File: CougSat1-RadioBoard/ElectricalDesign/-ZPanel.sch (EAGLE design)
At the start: 0 parts

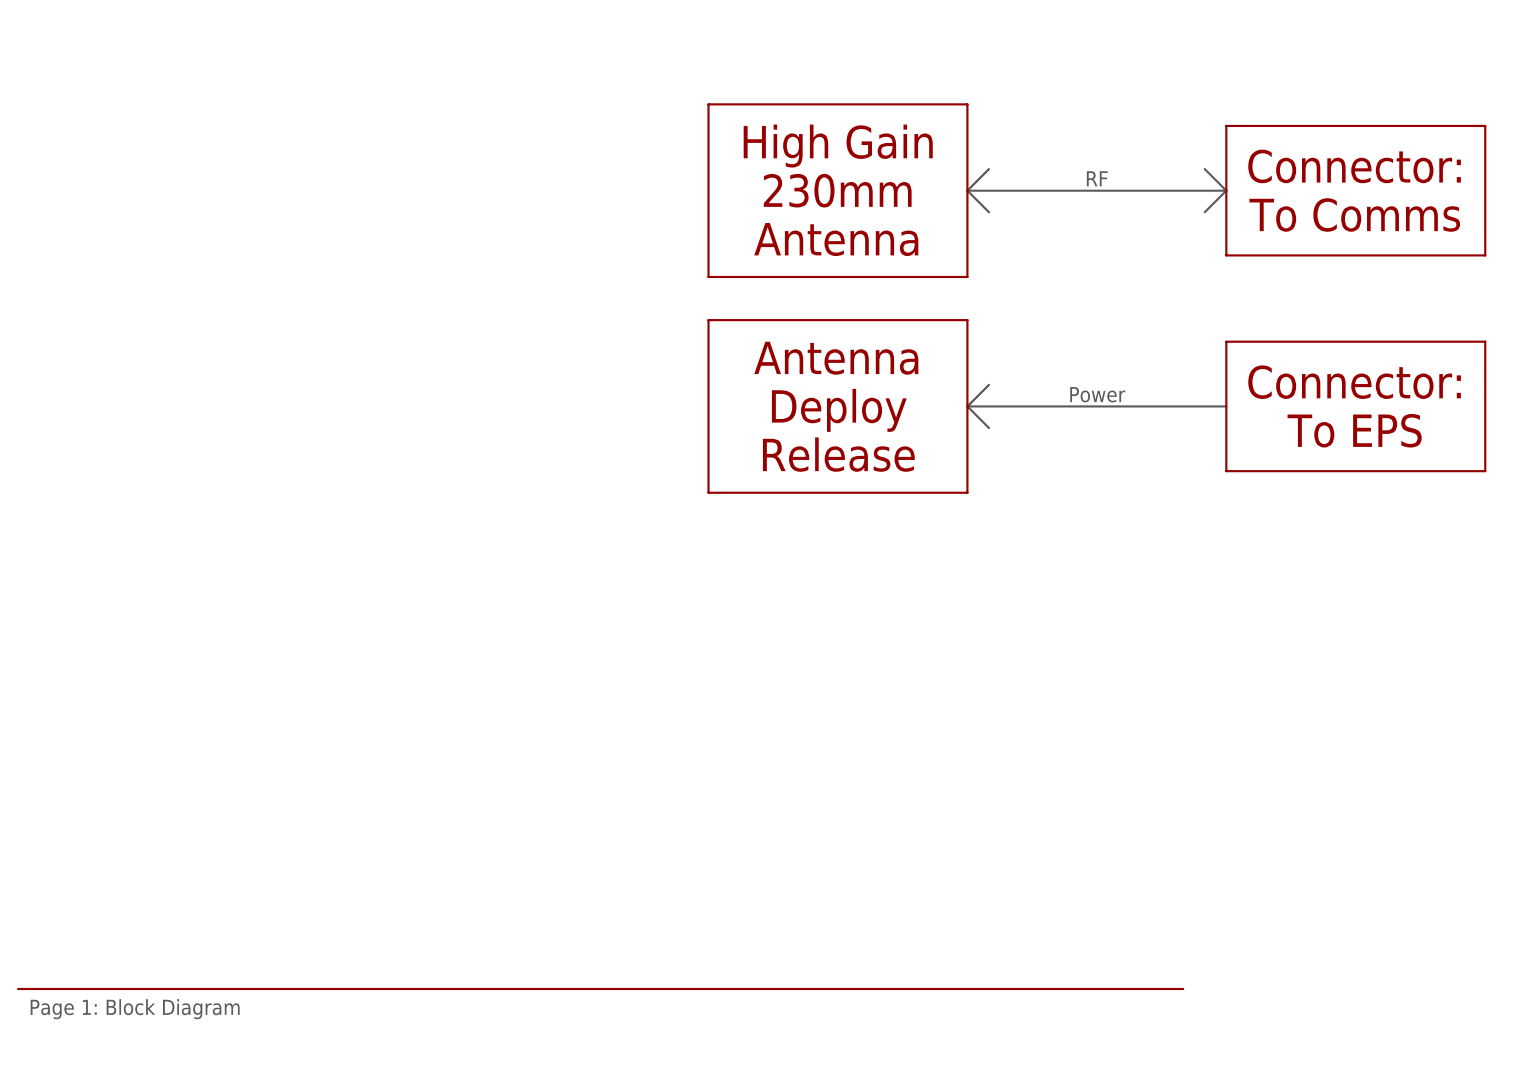
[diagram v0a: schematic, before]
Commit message: Added Photodiodes
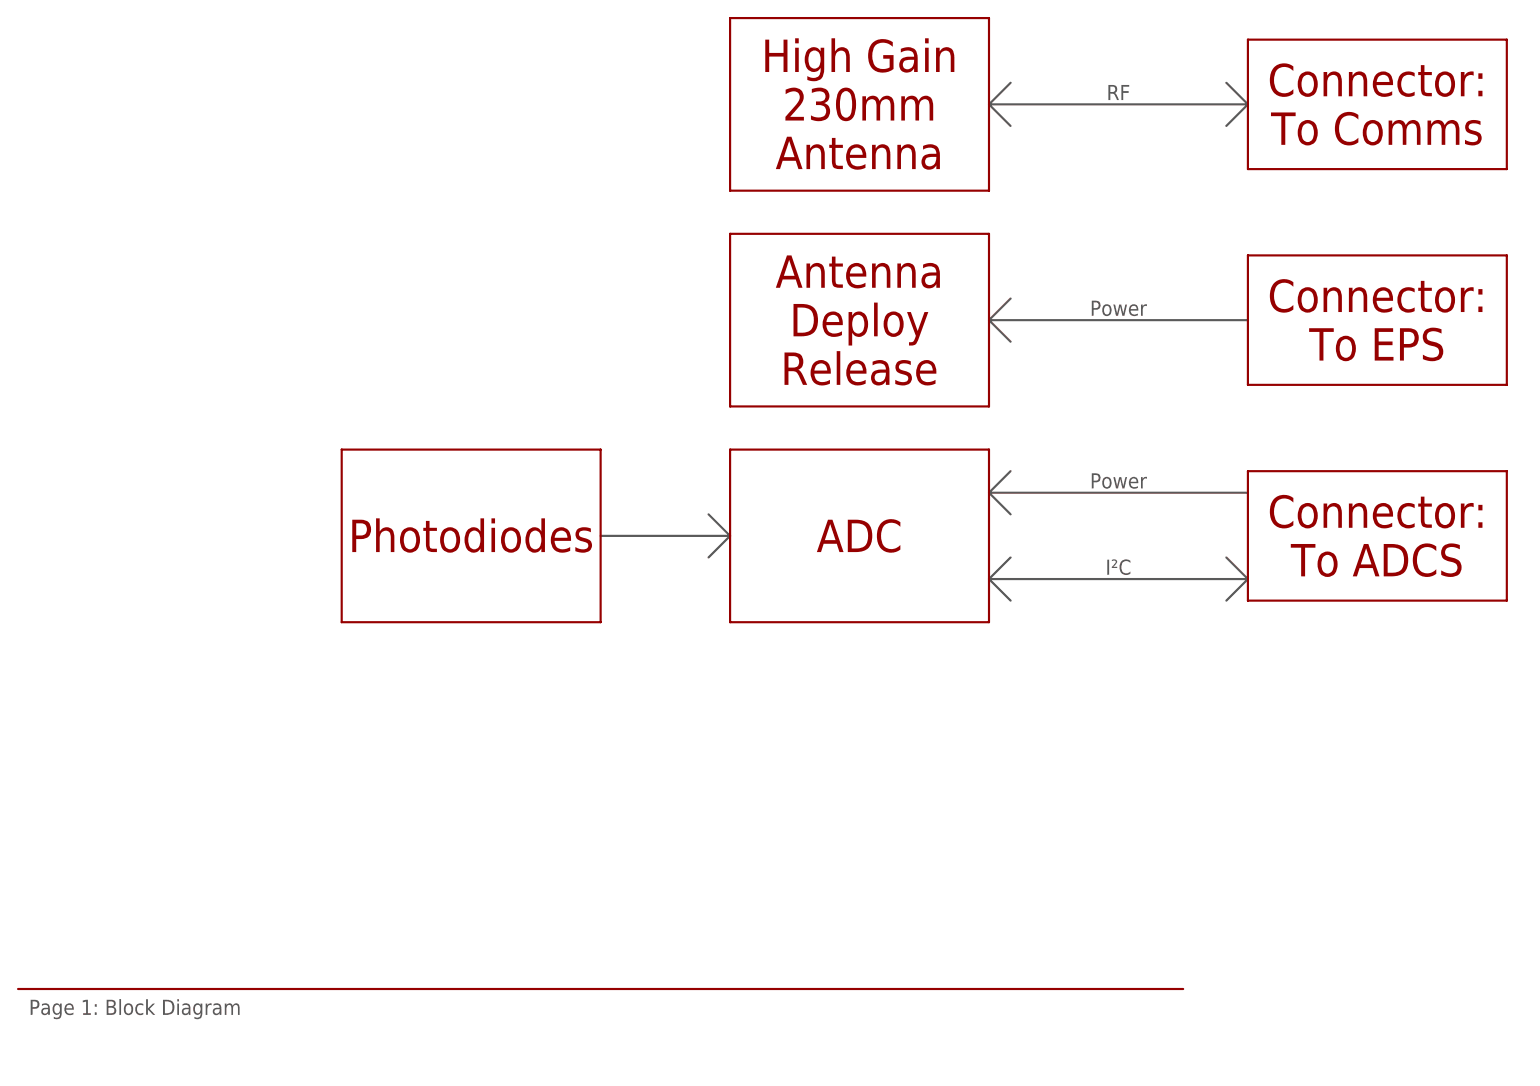
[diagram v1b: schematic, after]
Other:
- note added: "ADC"
- note added: "Connector: To ADCS"
- note added: "I²C"
- note added: "Photodiodes"
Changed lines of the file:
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@@
 <?xml version="1.0" encoding="utf-8"?>
 <!DOCTYPE eagle SYSTEM "eagle.dtd">
-<eagle version="9.2.1">
+<eagle version="9.2.2">
 <drawing>
 <settings>
@@
 <wire x1="137.16" y1="25.4" x2="0" y2="25.4" width="0.254" layer="94"/>
 <text x="1.27" y="24.13" size="1.778" layer="97" align="top-left">Page 1: Block Diagram</text>
-<text x="96.52" y="119.38" size="3.81" layer="94" align="center">High Gain
+<text x="99.06" y="129.54" size="3.81" layer="94" align="center">High Gain
 230mm
 Antenna</text>
-<text x="96.52" y="93.98" size="3.81" layer="94" align="center">Antenna
+<text x="99.06" y="104.14" size="3.81" layer="94" align="center">Antenna
 Deploy
 Release</text>
-<text x="157.48" y="119.38" size="3.81" layer="94" align="center">Connector:
+<text x="160.02" y="129.54" size="3.81" layer="94" align="center">Connector:
 To Comms</text>
-<text x="157.48" y="93.98" size="3.81" layer="94" align="center">Connector:
+<text x="160.02" y="104.14" size="3.81" layer="94" align="center">Connector:
 To EPS</text>
-<wire x1="142.24" y1="127" x2="172.72" y2="127" width="0.254" layer="94"/>
-<wire x1="172.72" y1="127" x2="172.72" y2="111.76" width="0.254" layer="94"/>
-<wire x1="172.72" y1="111.76" x2="142.24" y2="111.76" width="0.254" layer="94"/>
-<wire x1="142.24" y1="111.76" x2="142.24" y2="127" width="0.254" layer="94"/>
-<wire x1="142.24" y1="101.6" x2="142.24" y2="86.36" width="0.254" layer="94"/>
-<wire x1="142.24" y1="86.36" x2="172.72" y2="86.36" width="0.254" layer="94"/>
-<wire x1="172.72" y1="86.36" x2="172.72" y2="101.6" width="0.254" layer="94"/>
-<wire x1="172.72" y1="101.6" x2="142.24" y2="101.6" width="0.254" layer="94"/>
-<wire x1="81.28" y1="129.54" x2="111.76" y2="129.54" width="0.254" layer="94"/>
-<wire x1="111.76" y1="129.54" x2="111.76" y2="109.22" width="0.254" layer="94"/>
-<wire x1="111.76" y1="109.22" x2="81.28" y2="109.22" width="0.254" layer="94"/>
-<wire x1="81.28" y1="109.22" x2="81.28" y2="129.54" width="0.254" layer="94"/>
-<wire x1="81.28" y1="104.14" x2="111.76" y2="104.14" width="0.254" layer="94"/>
-<wire x1="81.28" y1="104.14" x2="81.28" y2="83.82" width="0.254" layer="94"/>
-<wire x1="111.76" y1="104.14" x2="111.76" y2="83.82" width="0.254" layer="94"/>
-<wire x1="81.28" y1="83.82" x2="111.76" y2="83.82" width="0.254" layer="94"/>
-<wire x1="111.76" y1="119.38" x2="142.24" y2="119.38" width="0.254" layer="97"/>
-<wire x1="139.7" y1="121.92" x2="142.24" y2="119.38" width="0.254" layer="97"/>
-<wire x1="142.24" y1="119.38" x2="139.7" y2="116.84" width="0.254" layer="97"/>
-<wire x1="114.3" y1="121.92" x2="111.76" y2="119.38" width="0.254" layer="97"/>
-<wire x1="111.76" y1="119.38" x2="114.3" y2="116.84" width="0.254" layer="97"/>
-<wire x1="142.24" y1="93.98" x2="111.76" y2="93.98" width="0.254" layer="97"/>
-<wire x1="114.3" y1="96.52" x2="111.76" y2="93.98" width="0.254" layer="97"/>
-<wire x1="111.76" y1="93.98" x2="114.3" y2="91.44" width="0.254" layer="97"/>
-<text x="127" y="119.888" size="1.778" layer="97" align="bottom-center">RF</text>
-<text x="127" y="94.488" size="1.778" layer="97" align="bottom-center">Power</text>
+<wire x1="144.78" y1="137.16" x2="175.26" y2="137.16" width="0.254" layer="94"/>
+<wire x1="175.26" y1="137.16" x2="175.26" y2="121.92" width="0.254" layer="94"/>
+<wire x1="175.26" y1="121.92" x2="144.78" y2="121.92" width="0.254" layer="94"/>
+<wire x1="144.78" y1="121.92" x2="144.78" y2="137.16" width="0.254" layer="94"/>
+<wire x1="144.78" y1="111.76" x2="144.78" y2="96.52" width="0.254" layer="94"/>
+<wire x1="144.78" y1="96.52" x2="175.26" y2="96.52" width="0.254" layer="94"/>
+<wire x1="175.26" y1="96.52" x2="175.26" y2="111.76" width="0.254" layer="94"/>
+<wire x1="175.26" y1="111.76" x2="144.78" y2="111.76" width="0.254" layer="94"/>
+<wire x1="83.82" y1="139.7" x2="114.3" y2="139.7" width="0.254" layer="94"/>
+<wire x1="114.3" y1="139.7" x2="114.3" y2="119.38" width="0.254" layer="94"/>
+<wire x1="114.3" y1="119.38" x2="83.82" y2="119.38" width="0.254" layer="94"/>
+<wire x1="83.82" y1="119.38" x2="83.82" y2="139.7" width="0.254" layer="94"/>
+<wire x1="83.82" y1="114.3" x2="114.3" y2="114.3" width="0.254" layer="94"/>
+<wire x1="83.82" y1="114.3" x2="83.82" y2="93.98" width="0.254" layer="94"/>
+<wire x1="114.3" y1="114.3" x2="114.3" y2="93.98" width="0.254" layer="94"/>
+<wire x1="83.82" y1="93.98" x2="114.3" y2="93.98" width="0.254" layer="94"/>
+<wire x1="114.3" y1="129.54" x2="144.78" y2="129.54" width="0.254" layer="97"/>
+<wire x1="142.24" y1="132.08" x2="144.78" y2="129.54" width="0.254" layer="97"/>
+<wire x1="144.78" y1="129.54" x2="142.24" y2="127" width="0.254" layer="97"/>
+<wire x1="116.84" y1="132.08" x2="114.3" y2="129.54" width="0.254" layer="97"/>
+<wire x1="114.3" y1="129.54" x2="116.84" y2="127" width="0.254" layer="97"/>
+<wire x1="144.78" y1="104.14" x2="114.3" y2="104.14" width="0.254" layer="97"/>
+<wire x1="116.84" y1="106.68" x2="114.3" y2="104.14" width="0.254" layer="97"/>
+<wire x1="114.3" y1="104.14" x2="116.84" y2="101.6" width="0.254" layer="97"/>
+<text x="129.54" y="130.048" size="1.778" layer="97" align="bottom-center">RF</text>
+<text x="129.54" y="104.648" size="1.778" layer="97" align="bottom-center">Power</text>
+<text x="99.06" y="78.74" size="3.81" layer="94" align="center">ADC</text>
+<text x="160.02" y="78.74" size="3.81" layer="94" align="center">Connector:
+To ADCS</text>
+<wire x1="144.78" y1="86.36" x2="144.78" y2="71.12" width="0.254" layer="94"/>
+<wire x1="144.78" y1="71.12" x2="175.26" y2="71.12" width="0.254" layer="94"/>
+<wire x1="175.26" y1="71.12" x2="175.26" y2="86.36" width="0.254" layer="94"/>
+<wire x1="175.26" y1="86.36" x2="144.78" y2="86.36" width="0.254" layer="94"/>
+<wire x1="83.82" y1="88.9" x2="114.3" y2="88.9" width="0.254" layer="94"/>
+<wire x1="83.82" y1="88.9" x2="83.82" y2="68.58" width="0.254" layer="94"/>
+<wire x1="114.3" y1="88.9" x2="114.3" y2="68.58" width="0.254" layer="94"/>
+<wire x1="83.82" y1="68.58" x2="114.3" y2="68.58" width="0.254" layer="94"/>
+<wire x1="144.78" y1="83.82" x2="114.3" y2="83.82" width="0.254" layer="97"/>
+<wire x1="116.84" y1="86.36" x2="114.3" y2="83.82" width="0.254" layer="97"/>
+<wire x1="114.3" y1="83.82" x2="116.84" y2="81.28" width="0.254" layer="97"/>
+<text x="129.54" y="84.328" size="1.778" layer="97" align="bottom-center">Power</text>
+<wire x1="144.78" y1="73.66" x2="114.3" y2="73.66" width="0.254" layer="97"/>
+<wire x1="116.84" y1="76.2" x2="114.3" y2="73.66" width="0.254" layer="97"/>
+<wire x1="114.3" y1="73.66" x2="116.84" y2="71.12" width="0.254" layer="97"/>
+<text x="129.54" y="74.168" size="1.778" layer="97" align="bottom-center">I²C</text>
+<wire x1="144.78" y1="73.66" x2="142.24" y2="71.12" width="0.254" layer="97"/>
+<wire x1="142.24" y1="76.2" x2="144.78" y2="73.66" width="0.254" layer="97"/>
+<text x="53.34" y="78.74" size="3.81" layer="94" align="center">Photodiodes</text>
+<wire x1="38.1" y1="88.9" x2="68.58" y2="88.9" width="0.254" layer="94"/>
+<wire x1="38.1" y1="88.9" x2="38.1" y2="68.58" width="0.254" layer="94"/>
+<wire x1="68.58" y1="88.9" x2="68.58" y2="68.58" width="0.254" layer="94"/>
+<wire x1="38.1" y1="68.58" x2="68.58" y2="68.58" width="0.254" layer="94"/>
+<wire x1="83.82" y1="78.74" x2="68.58" y2="78.74" width="0.254" layer="97"/>
+<wire x1="83.82" y1="78.74" x2="81.28" y2="76.2" width="0.254" layer="97"/>
+<wire x1="81.28" y1="81.28" x2="83.82" y2="78.74" width="0.254" layer="97"/>
 </plain>
 <instances>

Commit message: Created Schematic and Design Document
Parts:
- added D1: SFH 2430, CougsInSpace-Sensors:PHOTODIODE-SFH2430
- added J1: High Gain Antenna, CougsInSpace-Connectors:COAX-U.FL
- added J2: Deployables, CougsInSpace-Connectors:1X04-PICOLOCK
- added J3: High Gain +, CougsInSpace-Connectors:1X01-THT-1.0
- added J4: ADCS, CougsInSpace-Connectors:1X04-PICOLOCK
- added J5: Flap +X, CougsInSpace-Connectors:1X01-5MM-SPRING-0990
- added J6: Flap -X, CougsInSpace-Connectors:1X01-5MM-SPRING-0990
- added J7: Flap +Y, CougsInSpace-Connectors:1X01-5MM-SPRING-0990
- added J8: Flap -Y, CougsInSpace-Connectors:1X01-5MM-SPRING-0990
- added R1, R2: 15Ω 5%, CougsInSpace-Resistors:RES-H-15R-THT-15MM
- added R3: 150Ω 1%, CougsInSpace-Resistors:RES-V-150R-1608
- added R4, R5, R6, R7, R8, R9: 0Ω <20mΩ, CougsInSpace-Resistors:RES-V-0-1608
- added U1: LTC2499, CougsInSpace-IC-Conversion:LTC2499
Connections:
- new net 3.3V: J4.3, R4.2, R5.2, R6.2, U1.VCC
- new net AGND: R3.1, U1.COM, U1.REF-
- new net AVDD: D1.C, U1.REF+
- new net DGND: R7.1, R8.1, R9.1, U1.CH0, U1.CH1, U1.CH10, U1.CH11, U1.CH12, U1.CH13, U1.CH14, U1.CH15, U1.CH2, U1.CH3, U1.CH4, U1.CH5, U1.CH6, U1.CH8, U1.CH9, U1.DGND, U1.F0
- new net I2C_SCL_ADCS: J4.2, U1.SCL
- new net I2C_SDA_ADCS: J4.1, U1.SDA
- new net N$1: D1.A, R3.2, U1.CH7
- new net N$10: R5.1, R8.2, U1.CA1
- new net N$11: R6.1, R9.2, U1.CA2
- new net N$2: J2.1, J2.2, R1.1, R2.1
- new net N$3: J2.4, R1.2, R2.2
- new net N$4: J1.CENTER, J3.1
- new net N$5: J2.3, J5.1, J6.1, J7.1, J8.1
- new net N$6: U1.ADCINP, U1.MUXOUTP
- new net N$7: U1.ADCINN, U1.MUXOUTN
- new net N$9: R4.1, R7.2, U1.CA0
- new net PGND: J4.4
- new net RFGND: J1.SHIELD
